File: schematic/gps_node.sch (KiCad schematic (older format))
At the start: 84 parts, among them IC1 MMA8452Q, IC2 MCP73831/2, J1 USB_OTG, J10 Mounting Hole, J11 TEST Vbatt, J12 Test 3.3v, J13 Test Gnd, J14 UART RF, J15 I2C GPS, J16 UART GPS, J17 GPIO_0, J18 GPIO_1, J2 AVR ICSP, J3 LIPO_BAT, J4 SOLAR, J5 FW_UPDATE, J6 SMA, J7 Mounting Hole, J8 Mounting Hole, J9 Mounting Hole, SW1 SW_SP3T, SW2 RESET, SW3 RESET, SW4 RESET, U1 TLV71333PDBV, U2 ublox-cam-m8q-0, U3 ATMEGA32U4-AU, U4 RN2483, Y1 16MHz

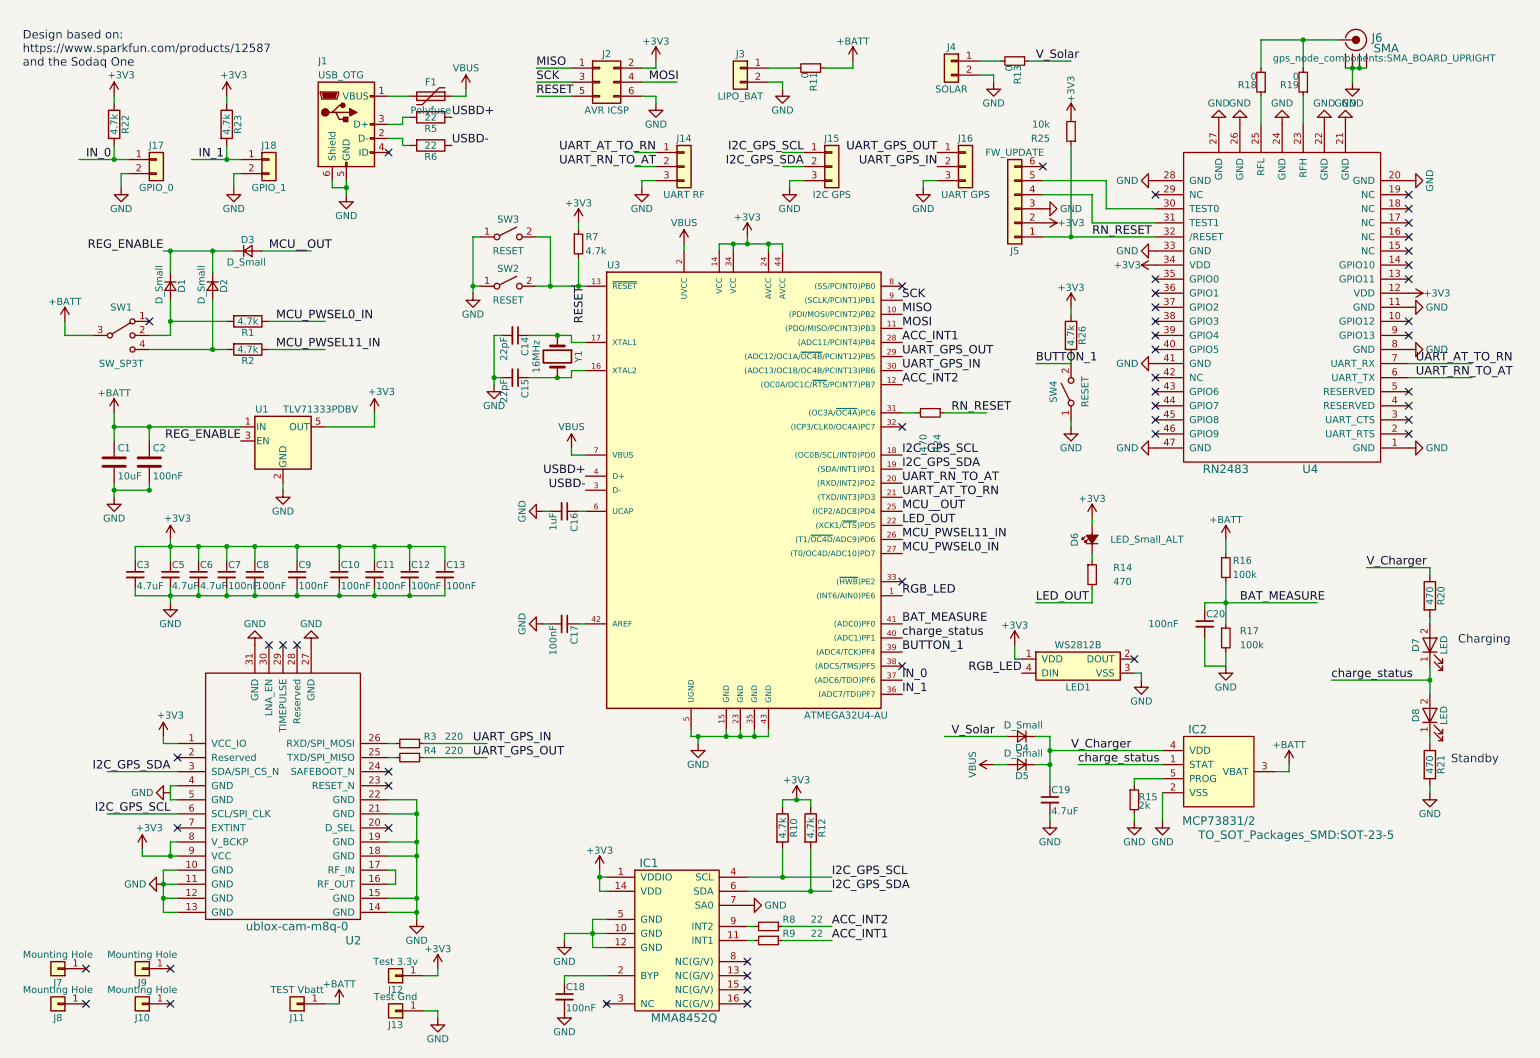
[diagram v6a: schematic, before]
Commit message: Simplify schematic
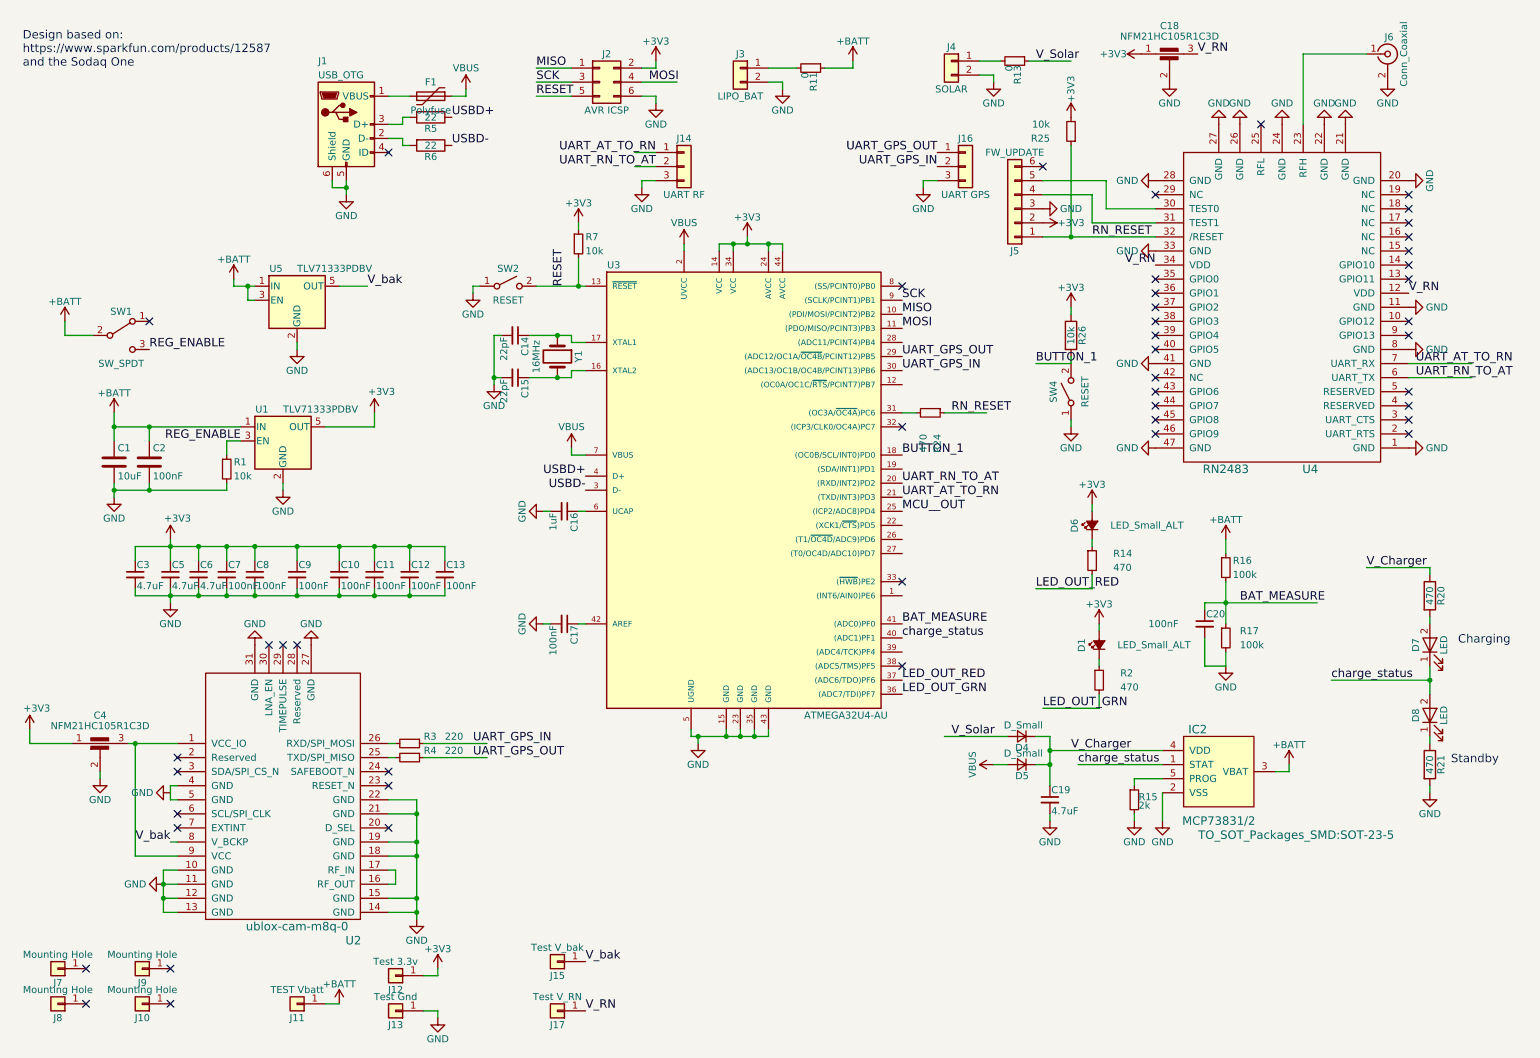
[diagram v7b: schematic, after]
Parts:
- removed C18: 100nF, Capacitors_SMD:C_0805, symbol C_Small
- removed D1, D2, D3: D_Small, gps_node_components:BAS70, symbol D_Small
- removed IC1: MMA8452Q, gps_node_components:MMA8452Q, symbol MMA8452Q
- removed J15: I2C GPS, Pin_Headers:Pin_Header_Straight_1x03_Pitch2.54mm, symbol Conn_01x03
- removed J17: GPIO_0, Pin_Headers:Pin_Header_Straight_1x02_Pitch2.54mm, symbol Conn_01x02
- removed J18: GPIO_1, Pin_Headers:Pin_Header_Straight_1x02_Pitch2.54mm, symbol Conn_01x02
- removed J6: SMA, gps_node_components:SMA_BOARD_UPRIGHT, symbol SMA
- removed LED1: WS2812B, LEDs:LED_WS2812B-PLCC4, symbol WS2812B
- removed R1, R10, R12, R2, R22, R23: 4.7k, Resistors_SMD:R_0805, symbol R
- removed R18, R19: 0, Resistors_SMD:R_0805, symbol R_Small
- removed R8, R9: 22, Resistors_SMD:R_0805, symbol R_Small
- removed SW1: SW_SP3T, gps_node_components:DP3T_switch, symbol SW_SP3T
- removed SW3: RESET, Buttons_Switches_SMD:SW_SPST_PTS645, symbol SW_SPST
- added C18, C4: NFM21HC105R1C3D, symbol C_Feedthrough
- added D1: LED_Small_ALT, LEDs:LED_0805, symbol LED_Small_ALT
- added J15: Test V_bak, Socket_Strips:Socket_Strip_Straight_1x01_Pitch2.54mm, symbol Conn_01x01
- added J17: Test V_RN, Socket_Strips:Socket_Strip_Straight_1x01_Pitch2.54mm, symbol Conn_01x01
- added J6: Conn_Coaxial, symbol Conn_Coaxial
- added R1: 10k, Resistors_SMD:R_0805, symbol R_Small
- added R2: 470, Resistors_SMD:R_0805, symbol R_Small
- added SW1: SW_SPDT, symbol SW_SPDT
- added U5: TLV71333PDBV, TO_SOT_Packages_SMD:SOT-23-5, symbol TLV71333PDBV
- R26, R7: value 4.7k -> 10k
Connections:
- net labels added: LED_OUT_GRN, LED_OUT_RED, V_RN, V_bak
- net labels removed: ACC_INT1, ACC_INT2, I2C_GPS_SCL, I2C_GPS_SDA, IN_0, IN_1, LED_OUT, MCU_PWSEL0_IN, MCU_PWSEL11_IN, RGB_LED
- wire segments 246 -> 199
- no-connect marks 50 -> 47
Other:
- moved on the sheet: D6, R14

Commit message: Start initial pcb layout
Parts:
- added C21: 100nF, Capacitors_SMD:C_0805, symbol C_Small
- C1: renamed from C4; footprint (none) -> gps_node_components:C_FEEDTHROUGH_0805
- C19: renamed from C18; footprint (none) -> gps_node_components:C_FEEDTHROUGH_0805
- J17: renamed from J6; footprint (none) -> gps_node_components:CONN-RF-UFL
- SW1: footprint (none) -> Pin_Headers:Pin_Header_Straight_1x03_Pitch2.54mm
- renumbered C19 to C18, C1 to C2, C2 to C4, D4 to D1, D5 to D2, D6 to D3, D1 to D4, D7 to D5, D8 to D6, IC2 to IC1, J7 to J1, J17 to J10, J2 to J11, J14 to J12, J3 to J13, J4 to J14, J16 to J15, J5 to J16, J8 to J2, J9 to J3, J10 to J4, J11 to J5, J1 to J6, J12 to J7, J13 to J8, J15 to J9, R25 to R10, R26 to R11, R14 to R12, R2 to R13, R15 to R14, R16 to R15, R17 to R16, R20 to R17, R21 to R18, R3 to R2, R4 to R3, R5 to R4, R6 to R5, R7 to R6, R11 to R7, R24 to R8, R13 to R9, SW4 to SW3, U5 to U3, U3 to U4, U4 to U5
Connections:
- wire segments 199 -> 209
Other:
- moved on the sheet: C12, C13, C3, C5
